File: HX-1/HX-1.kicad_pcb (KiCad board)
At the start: 2 copper layers, 45 x 90 mm, 89 parts, among them J1 USB_C_Receptacle_USB2.0_16P, J10 Conn_01x24, J12 USART, J2 Conn_01x02_Socket, J3 I2C, J4 SPI, J8 UART, J9 Conn_01x24, SW1 BOOT0, U1 STM32H723ZGT6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

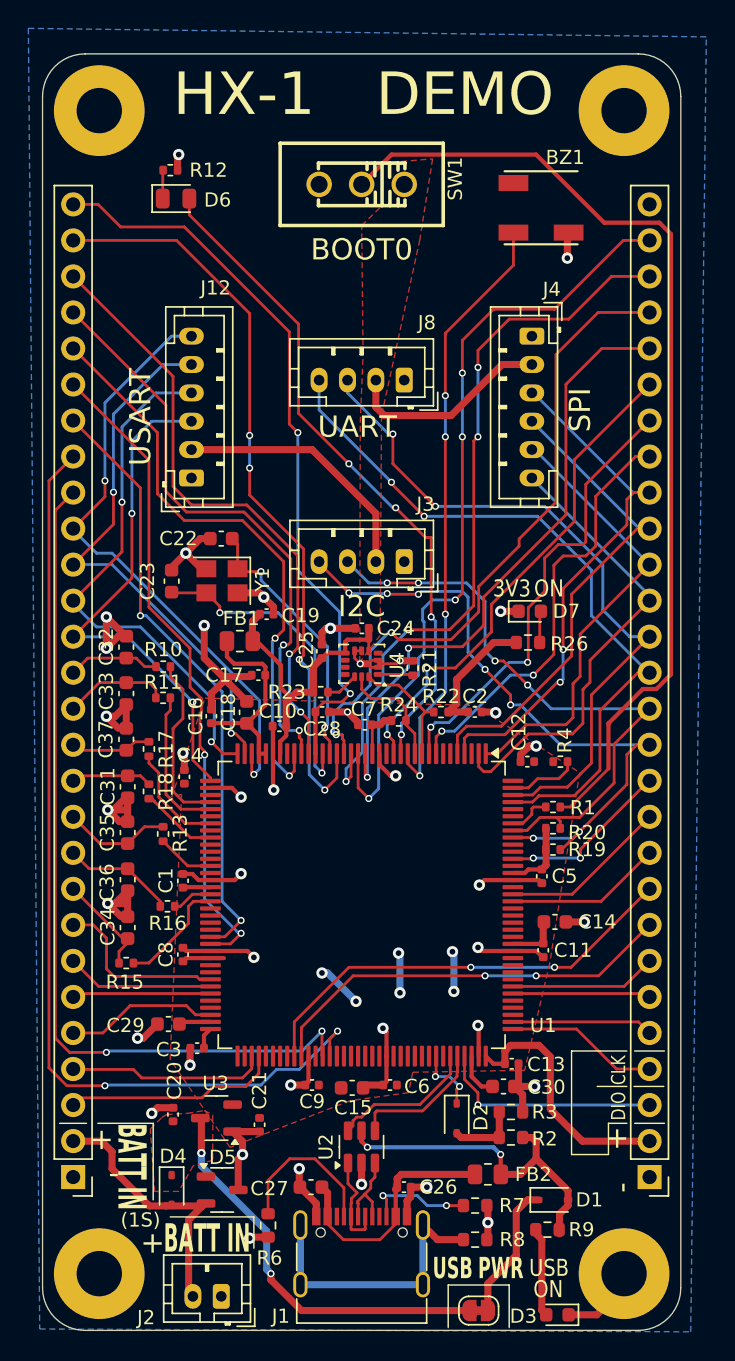
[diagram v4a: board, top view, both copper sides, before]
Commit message: flip TWM_PWM+1 and -1 for better routing, improve routing for better gnd planes
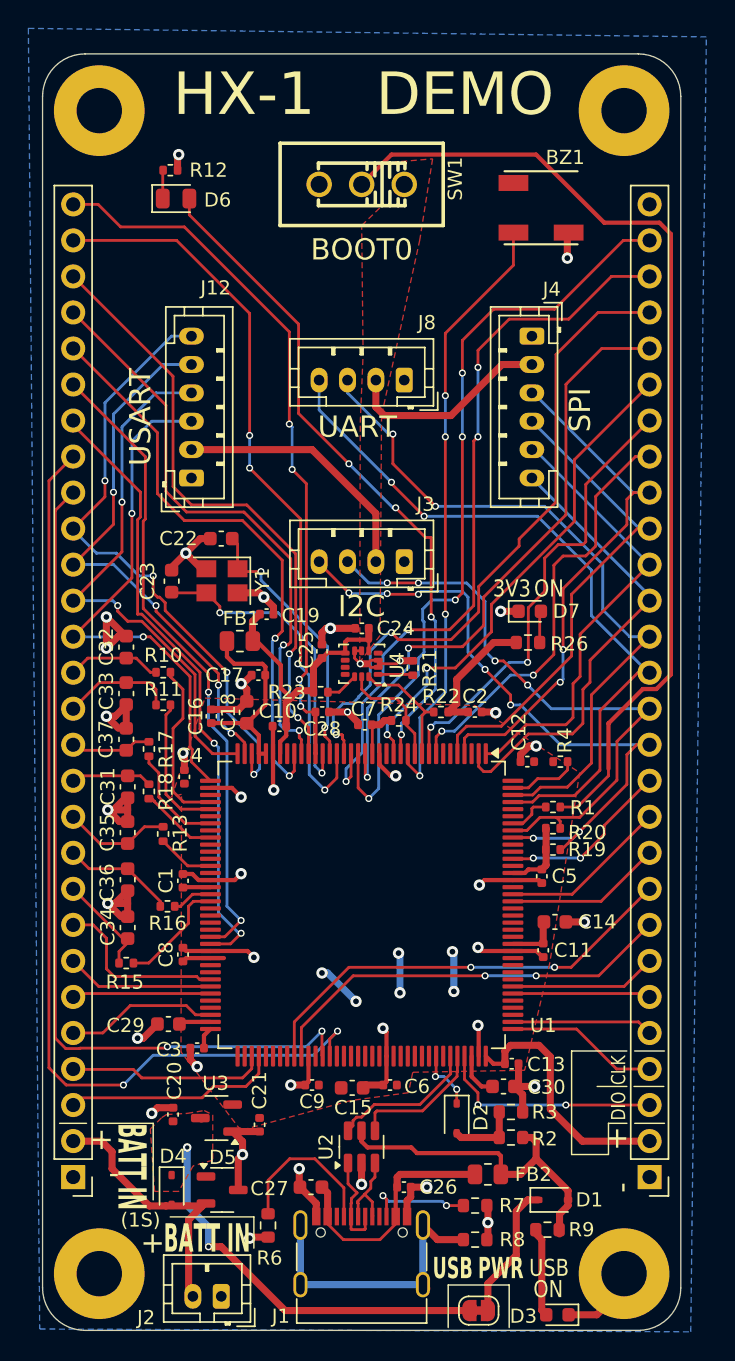
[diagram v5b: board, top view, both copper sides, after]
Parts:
- moved R11 0.50 mm to (135.5, 120.7)
- moved R10 0.40 mm to (135.5, 118.4)
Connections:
- J10 pad 22: /MCU/TIM1_PWM_1- -> /MCU/TIM1_PWM_1+
- J10 pad 23: /MCU/TIM1_PWM_1+ -> /MCU/TIM1_PWM_1-
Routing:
- net GND: track 138.4 -> 132.6 mm
- net /MCU/TIM1_PWM_1-: track 43.0 -> 45.5 mm
- net /MCU/TIM1_PWM_1+: track 46.2 -> 44.0 mm
- net /MCU/NRST: track 52.3 -> 50.3 mm, vias 2 -> 4
- net /MCU/USART2_RX: track 36.7 -> 37.7 mm
- net /MCU/USART2_TX: track 37.7 -> 38.6 mm
- net /MCU/USART2_CTS: track 43.6 -> 44.5 mm, vias 2 -> 4
- net /MCU/DAC_2_OUT: track 7.40 -> 7.90 mm
- net /MCU/USART2_RTS: track 38.9 -> 39.0 mm, vias 2 -> 4
- net /MCU/DEBUG_SWDIO: track 15.9 -> 16.0 mm, vias 1 -> 2
- net VBUS: vias 2 -> 0

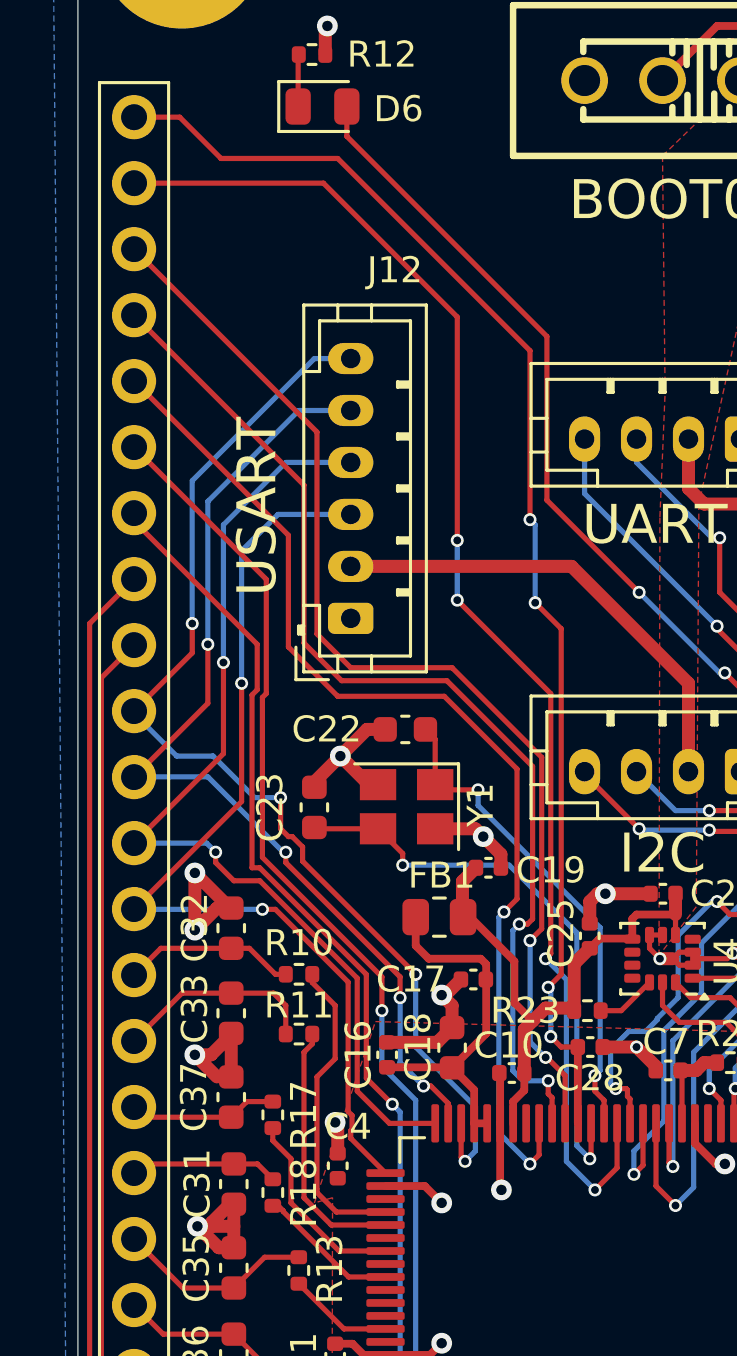
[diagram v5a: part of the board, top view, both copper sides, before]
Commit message: clean up left side traces, flip TWM1_PWM1 traces back as vias had them flipped
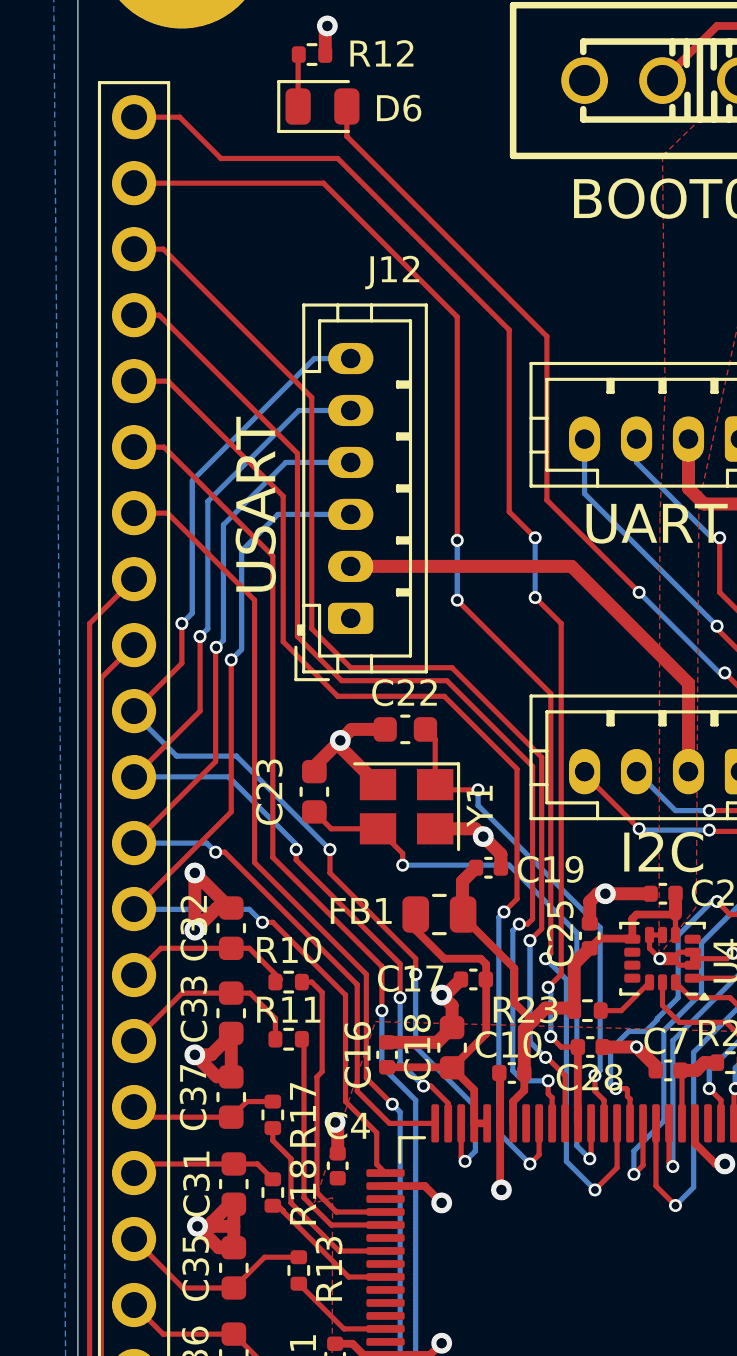
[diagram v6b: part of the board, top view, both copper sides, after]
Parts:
- moved C23 0.60 mm to (136.1, 111.4)
- moved R10 0.50 mm to (135.1, 118.7)
- moved R11 0.45 mm to (135.1, 120.9)
- moved FB1 0.10 mm to (140.9, 116.1)
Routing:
- net /MCU/GPIO_11: track 41.1 -> 41.9 mm
- net /MCU/GPIO_9: track 43.2 -> 43.9 mm
- net /MCU/GPIO_10: track 41.5 -> 42.1 mm
- net /MCU/TIM1_PWM_1-: track 45.5 -> 46.0 mm

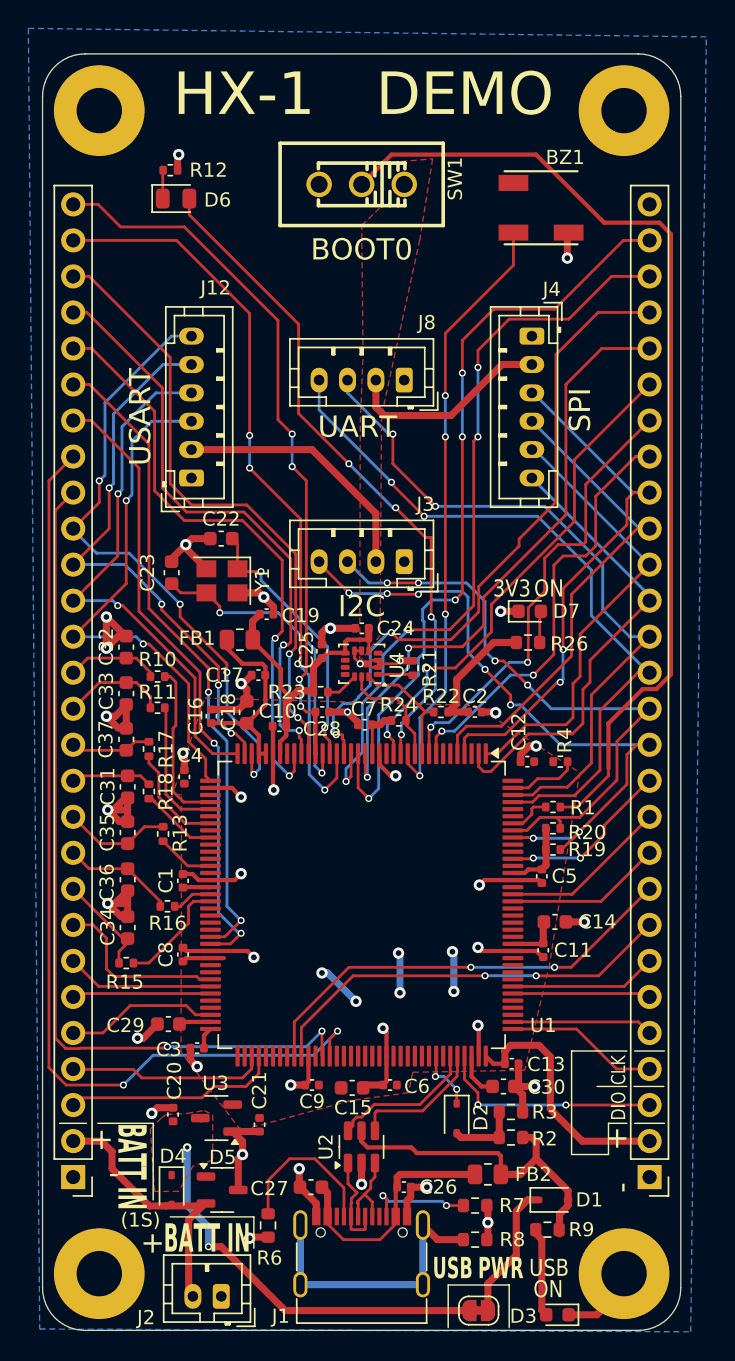
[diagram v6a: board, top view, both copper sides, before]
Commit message: generally improve gnd plane, reduce min gnd plane width to 0.2mm
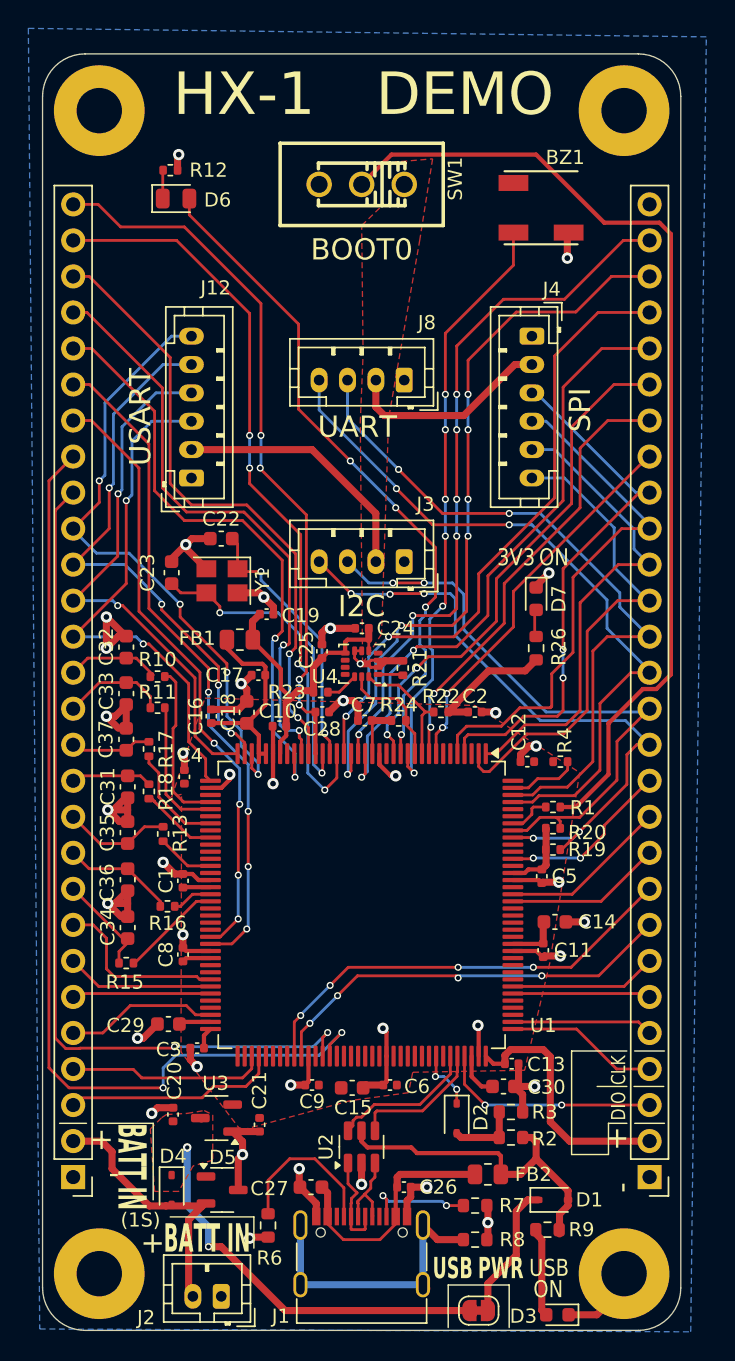
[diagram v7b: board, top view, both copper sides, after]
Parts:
- moved D7 1.00 mm to (161.8, 113.2), turned to -90 degrees
- moved R26 0.70 mm to (161.8, 116.7), turned to -90 degrees
- moved R21 0.70 mm to (152.4, 118.1)
- moved C7 0.30 mm to (149.7, 121.8)
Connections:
- J10 pad 22: /MCU/TIM1_PWM_1+ -> /MCU/TIM1_PWM_1-
- J10 pad 23: /MCU/TIM1_PWM_1- -> /MCU/TIM1_PWM_1+
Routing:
- net +3.3V: track 109.9 -> 100.4 mm, vias 6 -> 0
- net /MCU/GPIO_5: track 55.7 -> 49.9 mm, vias 4 -> 6
- net GND: track 132.8 -> 127.2 mm, vias 39 -> 38
- net /MCU/TIM1_PWM_1+: track 44.4 -> 47.2 mm, vias 2 -> 4
- net /MCU/TIM1_PWM_1-: track 46.0 -> 43.3 mm, vias 2 -> 4
- net /MCU/GPIO_1: track 30.2 -> 27.5 mm
- net /MCU/SPI4_CS: track 32.5 -> 34.9 mm
- net /MCU/SPI4_SCK: track 31.9 -> 34.0 mm
- net /MCU/SPI4_MOSI: track 34.9 -> 36.9 mm
- net /MCU/GPIO_7/DAC_EXT: track 46.7 -> 44.9 mm
- net /MCU/GPIO_3: track 35.0 -> 36.7 mm
- net /MCU/I2C_SCL: track 47.0 -> 45.6 mm, vias 7 -> 5
- net /MCU/TIM4_PWM_4: track 68.2 -> 69.5 mm
- net /MCU/SPI4_MISO: track 37.3 -> 38.4 mm
- net /MCU/ADC2_IN6: track 7.93 -> 7.23 mm
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
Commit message: further refine copper pours and traces, clean up Fab layer
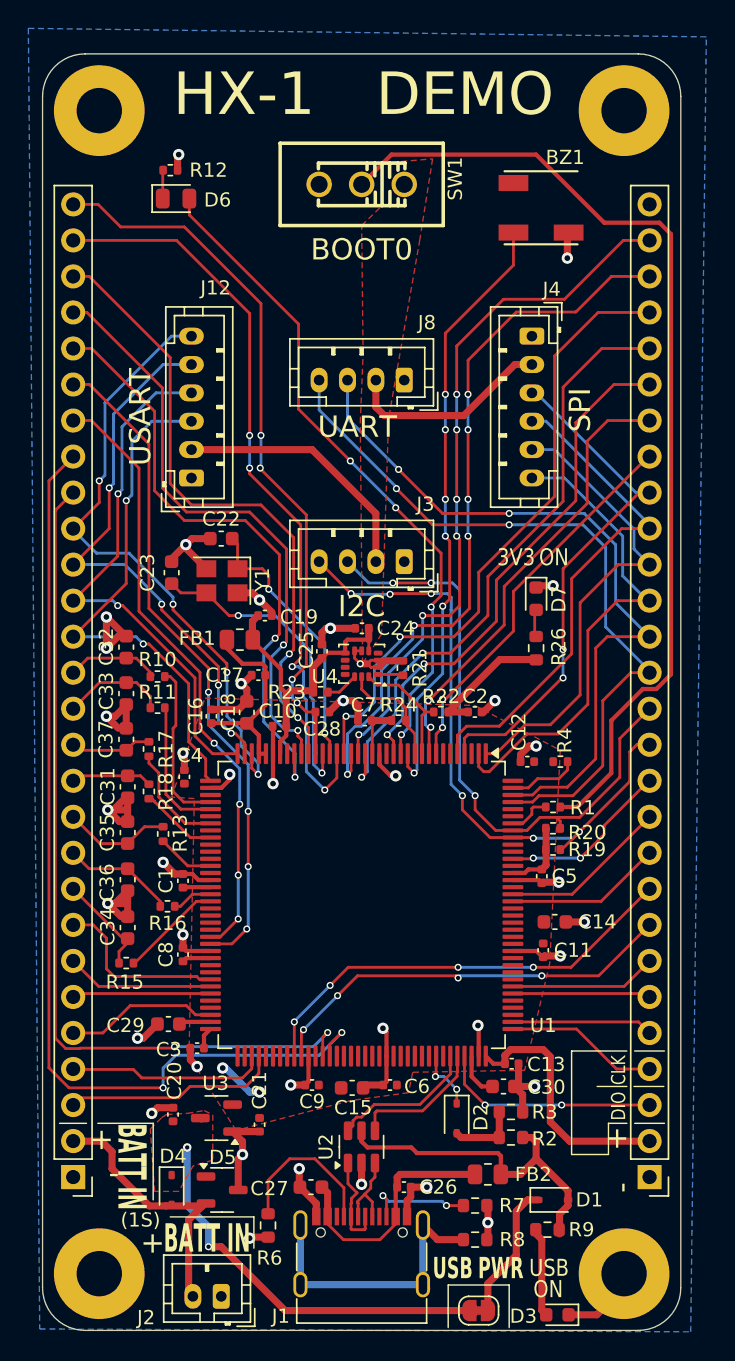
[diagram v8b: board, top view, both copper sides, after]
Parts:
- moved C19 0.16 mm to (142.7, 114.4)
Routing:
- net /MCU/UART8_RX: track 50.6 -> 52.6 mm
- net /MCU/UART8_TX: track 49.8 -> 51.6 mm
- net /MCU/SPI4_MISO: track 38.4 -> 37.0 mm
- net /MCU/SPI4_MOSI: track 36.9 -> 35.6 mm
- net /MCU/I2C_SDA: track 42.9 -> 43.9 mm, vias 2 -> 3
- net /MCU/GPIO_9: track 43.9 -> 44.8 mm
- net /MCU/SPI4_SCK: track 34.0 -> 33.4 mm
- net /MCU/GPIO_8: track 53.4 -> 54.0 mm
- net +3.3V: track 100.4 -> 99.9 mm, vias 0 -> 2
- net /MCU/I2C_SCL: track 45.6 -> 45.5 mm, vias 5 -> 6
